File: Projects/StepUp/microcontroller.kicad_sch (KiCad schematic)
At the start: 1 part, among them U2 RP2040

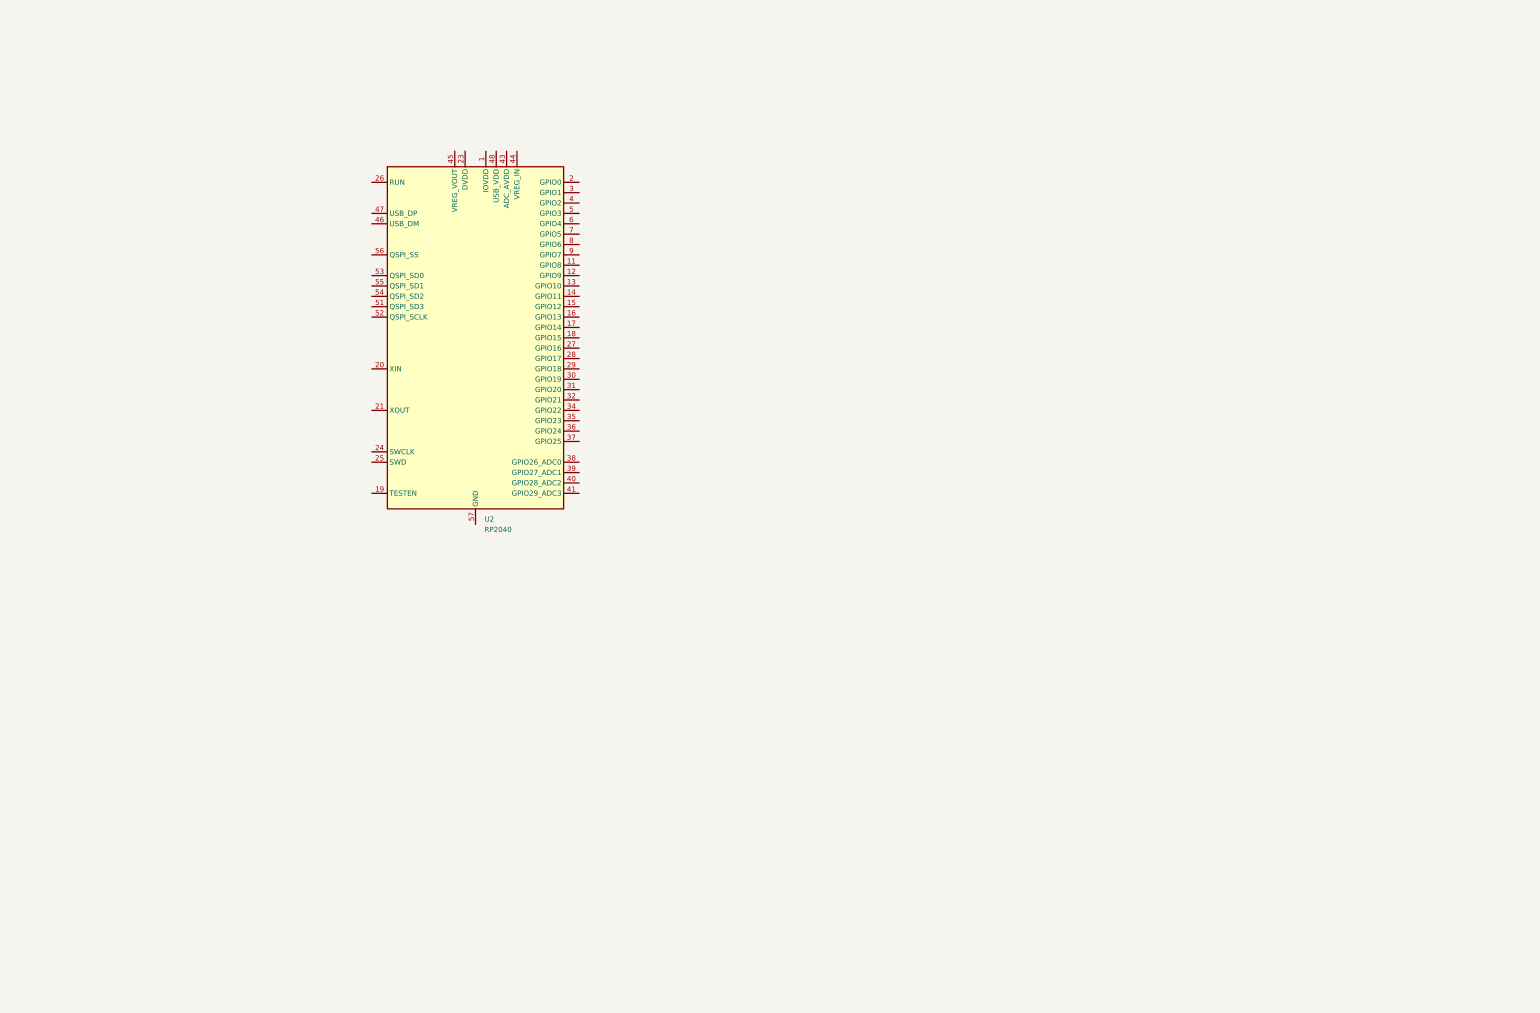
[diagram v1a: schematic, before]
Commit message: feat(rp2040): Layout begins, extra libraries
RPico minimal project downloaded + assets copied. Boost converter layout
in progress, 18650 battery holder added.
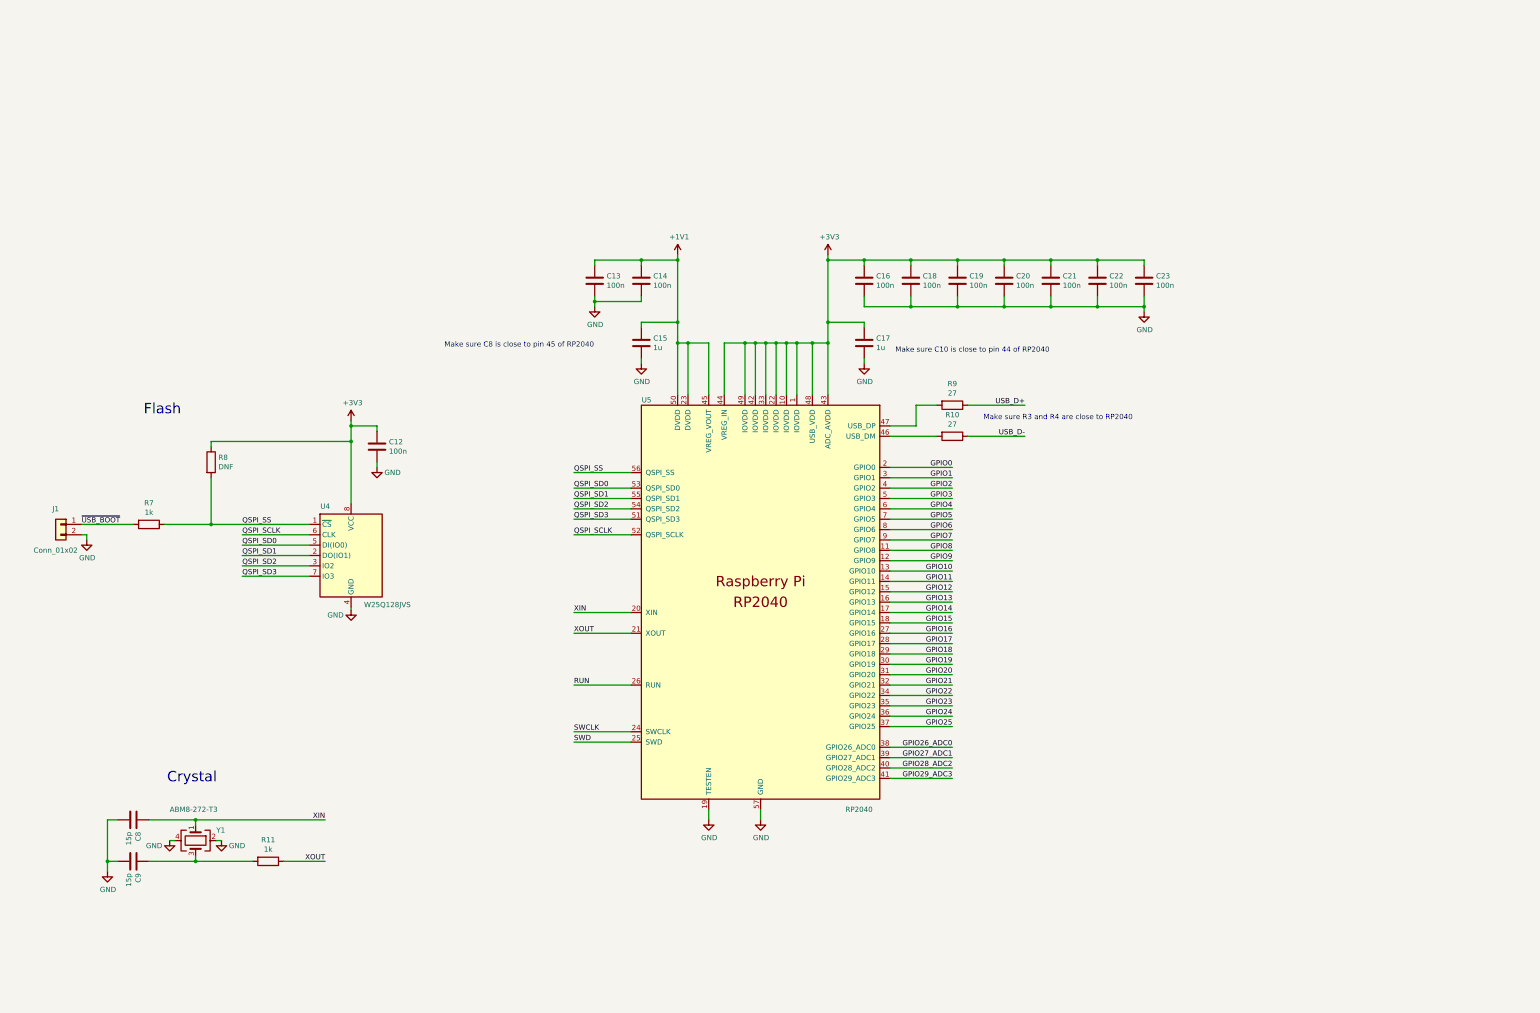
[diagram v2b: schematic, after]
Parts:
- removed U2: RP2040, Package_DFN_QFN:QFN-56-1EP_7x7mm_P0.4mm_EP3.2x3.2mm, symbol MCU_RaspberryPi:RP2040
- added C12, C13, C14, C16, C18, C19, C20, C21, C22, C23: 100n, Capacitor_SMD:C_0402_1005Metric, symbol Device:C
- added C15, C17: 1u, Capacitor_SMD:C_0402_1005Metric, symbol Device:C
- added C8, C9: 15p, Capacitor_SMD:C_0402_1005Metric, symbol Device:C
- added J1: Conn_01x02, Connector_PinHeader_2.54mm:PinHeader_1x02_P2.54mm_Vertical, symbol Connector_Generic:Conn_01x02
- added R10, R9: 27, Resistor_SMD:R_0402_1005Metric, symbol Device:R
- added R11, R7: 1k, Resistor_SMD:R_0402_1005Metric, symbol Device:R
- added R8: DNF, Resistor_SMD:R_0402_1005Metric, symbol Device:R
- added U4: W25Q128JVS, Package_SO:SOIC-8_5.23x5.23mm_P1.27mm, symbol Memory_Flash:W25Q128JVS
- added U5: RP2040, RP2040_minimal_r2:RP2040-QFN-56, symbol MCU_RaspberryPi_RP2040:RP2040
- added Y1: ABM8-272-T3, Crystal:Crystal_SMD_3225-4Pin_3.2x2.5mm, symbol Device:Crystal_GND24
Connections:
- new net: R10.2, U5.46 (USB_DM)
- new net: R9.2, U5.47 (USB_DP)
- new net: C9.1, R11.2, Y1.3
- new net +1V1: C13.1, C14.1, C15.1, U5.23 (DVDD), U5.45 (VREG_VOUT), U5.50 (DVDD)
- new net +3V3: C12.1, C16.1, C17.1, C18.1, C19.1, C20.1, C21.1, C22.1, C23.1, R8.1, U4.8 (VCC), U5.1 (IOVDD), U5.10 (IOVDD), U5.22 (IOVDD), U5.33 (IOVDD), U5.42 (IOVDD), U5.43 (ADC_AVDD), U5.44 (VREG_IN), U5.48 (USB_VDD), U5.49 (IOVDD)
- new net GND: C12.2, C13.2, C14.2, C15.2, C16.2, C17.2, C18.2, C19.2, C20.2, C21.2, C22.2, C23.2, C8.2, C9.2, J1.2 (Pin_2), U4.4 (GND), U5.19 (TESTEN), U5.57 (GND), Y1.2, Y1.4
- new net GPIO0: U5.2 (GPIO0)
- new net GPIO1: U5.3 (GPIO1)
- new net GPIO10: U5.13 (GPIO10)
- new net GPIO11: U5.14 (GPIO11)
- new net GPIO12: U5.15 (GPIO12)
- new net GPIO13: U5.16 (GPIO13)
- new net GPIO14: U5.17 (GPIO14)
- new net GPIO15: U5.18 (GPIO15)
- new net GPIO16: U5.27 (GPIO16)
- new net GPIO17: U5.28 (GPIO17)
- new net GPIO18: U5.29 (GPIO18)
- new net GPIO19: U5.30 (GPIO19)
- new net GPIO2: U5.4 (GPIO2)
- new net GPIO20: U5.31 (GPIO20)
- new net GPIO21: U5.32 (GPIO21)
- new net GPIO22: U5.34 (GPIO22)
- new net GPIO23: U5.35 (GPIO23)
- new net GPIO24: U5.36 (GPIO24)
- new net GPIO25: U5.37 (GPIO25)
- new net GPIO26_ADC0: U5.38 (GPIO26_ADC0)
- new net GPIO27_ADC1: U5.39 (GPIO27_ADC1)
- new net GPIO28_ADC2: U5.40 (GPIO28_ADC2)
- new net GPIO29_ADC3: U5.41 (GPIO29_ADC3)
- new net GPIO3: U5.5 (GPIO3)
- new net GPIO4: U5.6 (GPIO4)
- new net GPIO5: U5.7 (GPIO5)
- new net GPIO6: U5.8 (GPIO6)
- new net GPIO7: U5.9 (GPIO7)
- new net GPIO8: U5.11 (GPIO8)
- new net GPIO9: U5.12 (GPIO9)
- new net QSPI_SCLK: U4.6 (CLK), U5.52 (QSPI_SCLK)
- new net QSPI_SD0: U4.5 (DI(IO0)), U5.53 (QSPI_SD0)
- new net QSPI_SD1: U4.2 (DO(IO1)), U5.55 (QSPI_SD1)
- new net QSPI_SD2: U4.3 (IO2), U5.54 (QSPI_SD2)
- new net QSPI_SD3: U4.7 (IO3), U5.51 (QSPI_SD3)
- new net QSPI_SS: R7.1, R8.2, U4.1 (~{CS}), U5.56 (QSPI_SS)
- new net RUN: U5.26 (RUN)
- new net SWCLK: U5.24 (SWCLK)
- new net SWD: U5.25 (SWD)
- new net USB_D+: R9.1
- new net USB_D-: R10.1
- new net XIN: C8.1, U5.20 (XIN), Y1.1
- new net XOUT: R11.1, U5.21 (XOUT)
- new net ~{USB_BOOT}: J1.1 (Pin_1), R7.2
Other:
- note added: "Crystal"
- note added: "Flash"
- note added: "Make sure C10 is close to pin 44 of RP2040"
- note added: "Make sure C8 is close to pin 45 of RP2040"
- note added: "Make sure R3 and R4 are close to RP2040"

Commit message: feat(power): Input stage updates
USB vs Vbat source selection using PMOS gate logic.
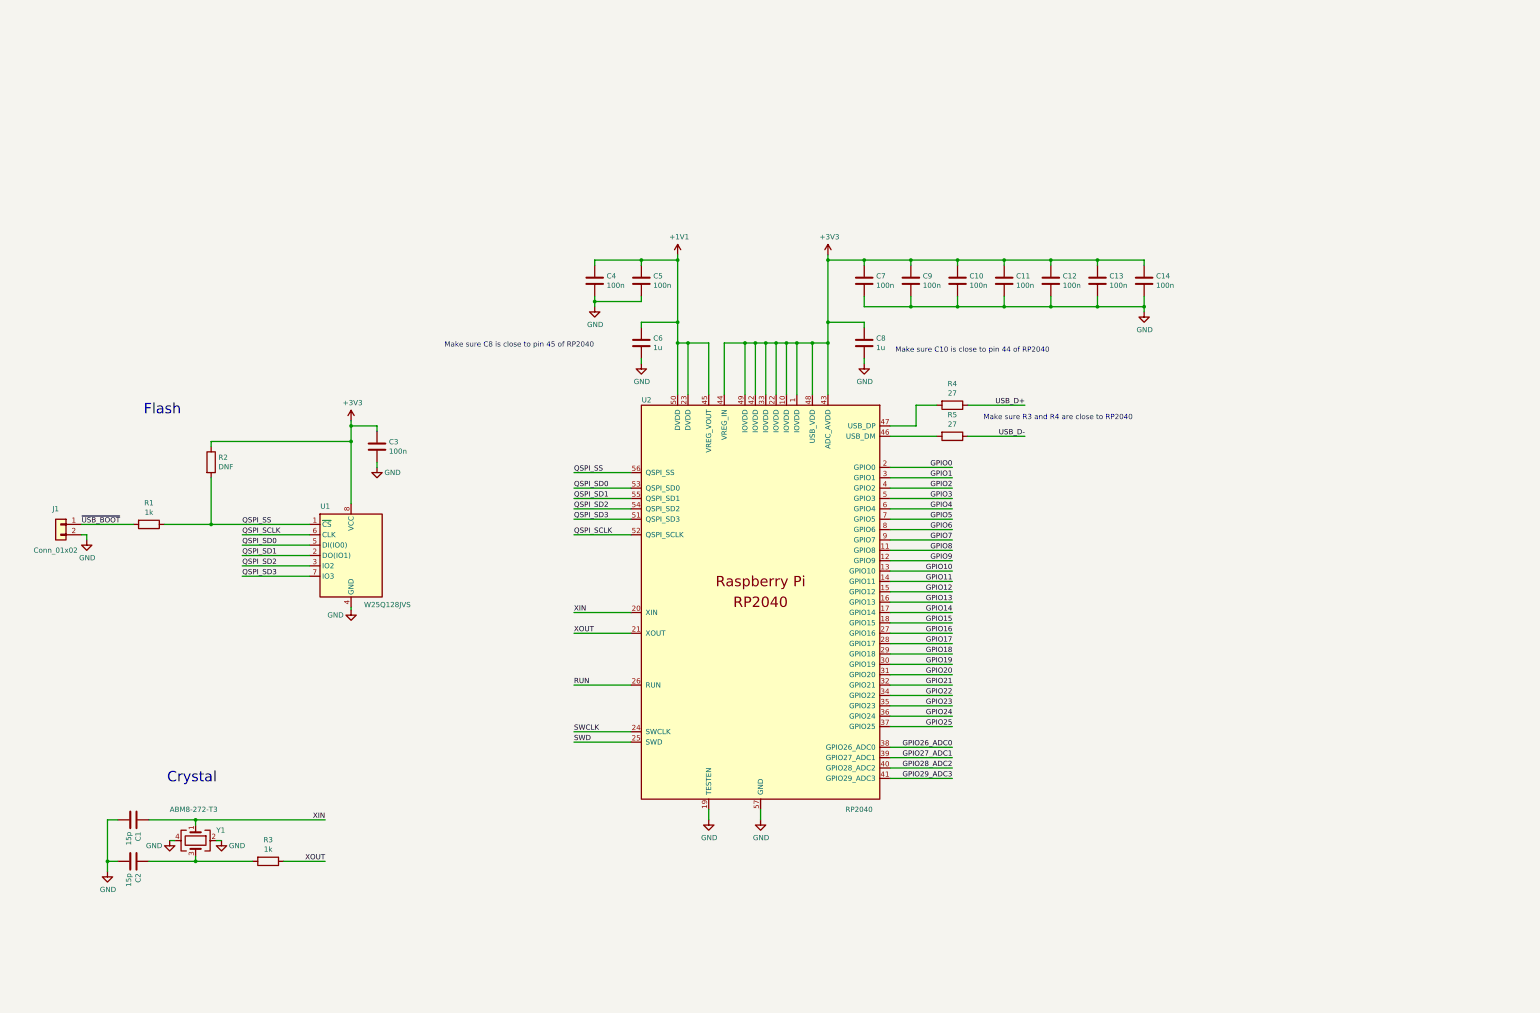
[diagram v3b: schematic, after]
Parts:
- renumbered C8 to C1, C19 to C10, C20 to C11, C21 to C12, C22 to C13, C23 to C14, C9 to C2, C12 to C3, C13 to C4, C14 to C5, C15 to C6, C16 to C7, C17 to C8, C18 to C9, R7 to R1, R8 to R2, R11 to R3, R9 to R4, R10 to R5, U4 to U1, U5 to U2

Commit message: feat(stepup): Many additions
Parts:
- removed J1: Conn_01x02, Connector_PinHeader_2.54mm:PinHeader_1x02_P2.54mm_Vertical, symbol Connector_Generic:Conn_01x02
- added D5: 1N4148W-TP, digikey-footprints:SOD-123, symbol dk_Diodes-Rectifiers-Single:1N4148W-TP
- added SW1, SW2: SW_Push, Button_Switch_SMD:SW_Push_1P1T_NO_Vertical_Wuerth_434133025816, symbol Switch:SW_Push
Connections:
- net GND: now also SW1.1, SW2.1
- net RUN: now also SW2.2
- net ~{USB_BOOT}: now also D5.A
- net GPIO22 renamed JOYSTSICK_BUTTON
- net GPIO25 renamed VUSB_monitor
- net GPIO26_ADC0 renamed JOYSTSICK_AXIS_V
- net GPIO27_ADC1 renamed JOYSTSICK_AXIS_H
- net GPIO28_ADC2 renamed Vbat_monitor
- new net: D5.K, SW1.2
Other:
- note added: "Flash memory"
- note added: "Make sure C6 is close to pin 45 of RP2040"
- note added: "Make sure these resistors are close to RP2040"
- note added: "Run - resets MCU USB_BOOT - hold this and toggle Run to enumerate as USB device for UF2 firmware upload"
- note removed: "Flash"
- note removed: "Make sure C8 is close to pin 45 of RP2040"
- note removed: "Make sure R3 and R4 are close to RP2040"
- moved on the sheet: C1, C2, C3, R1, R2, R3, U1, Y1

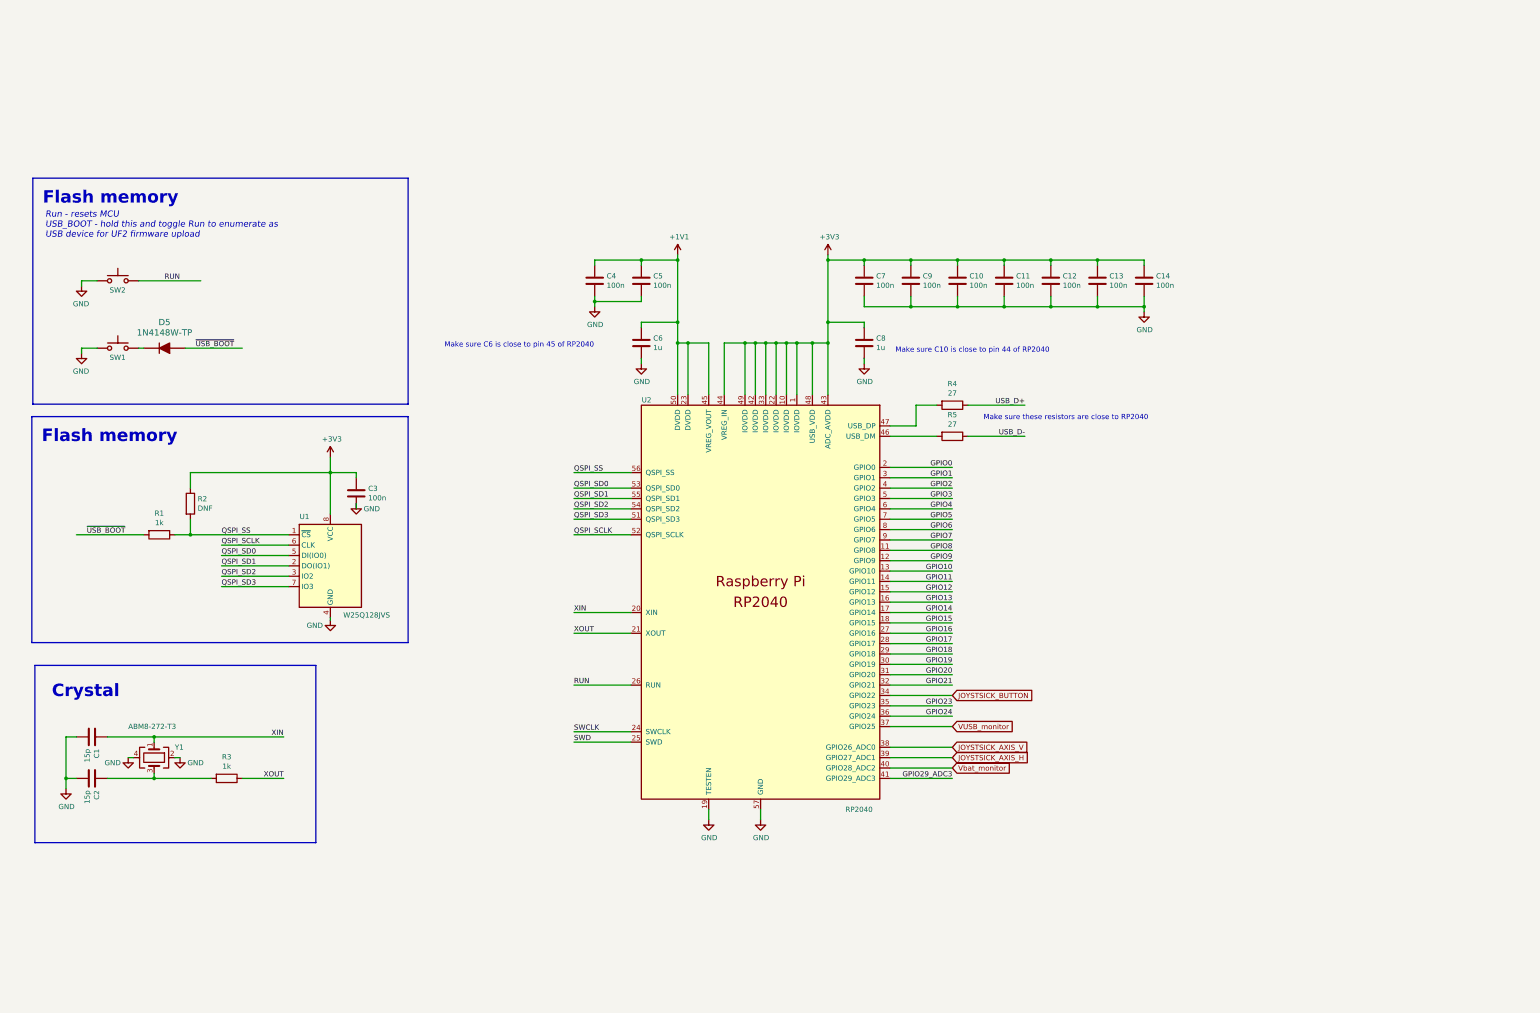
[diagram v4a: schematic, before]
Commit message: feat(stepup): Schematic + PCB updates
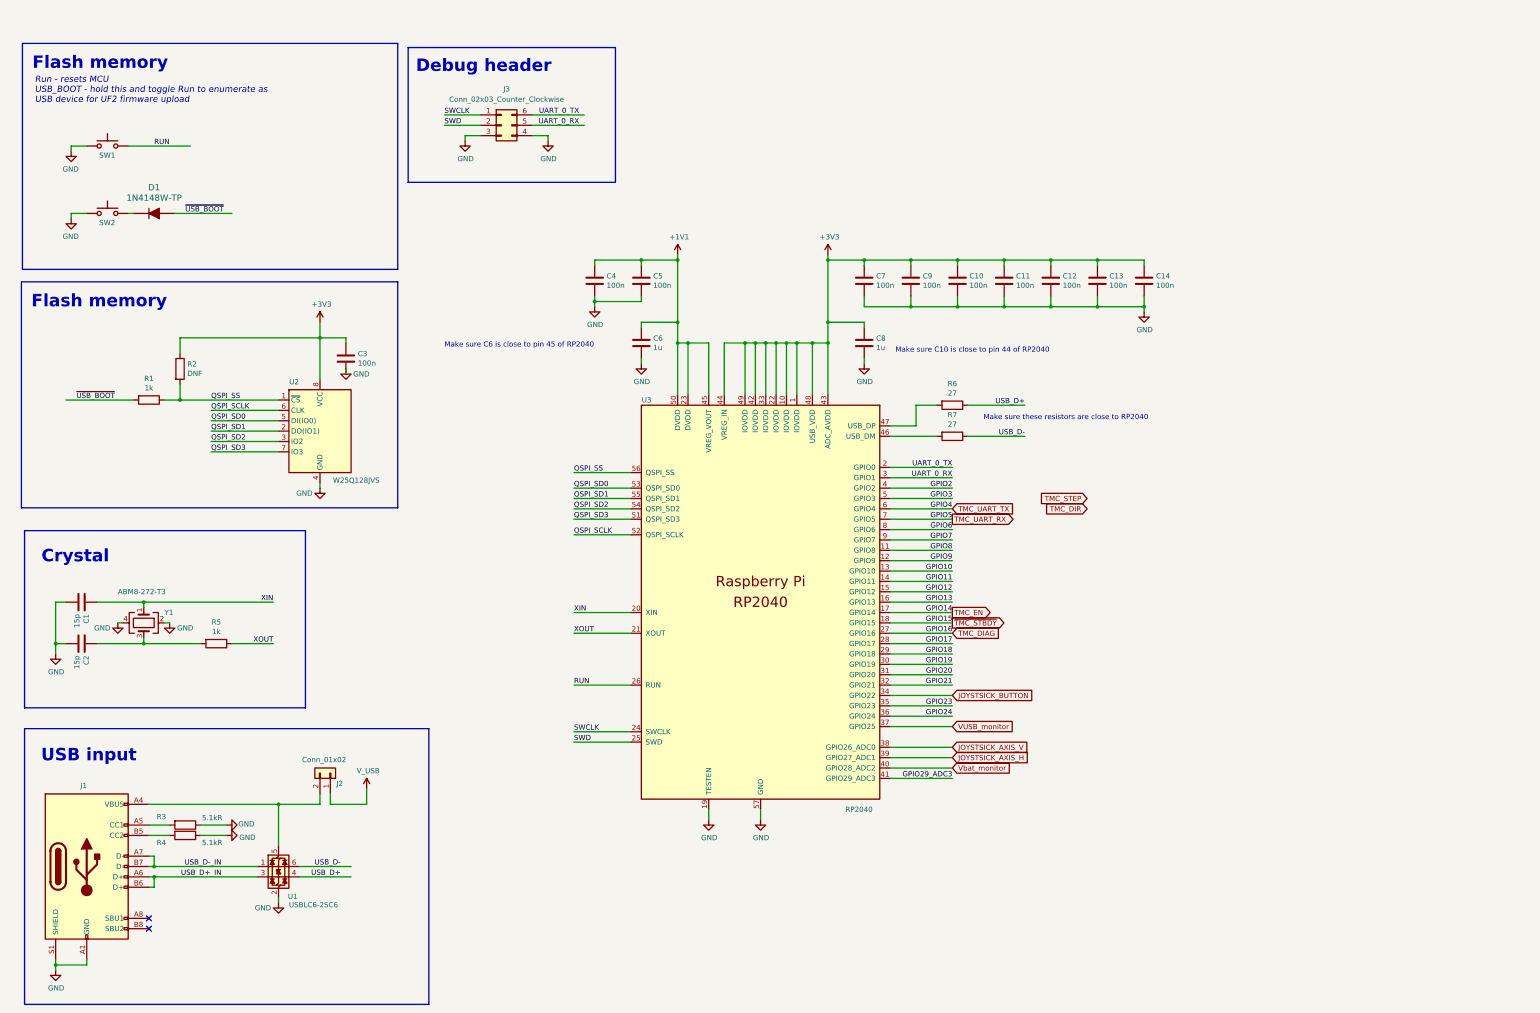
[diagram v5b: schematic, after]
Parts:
- added J1: USB_C_Receptacle_USB2.0_16P, Connector_USB:USB_C_Receptacle_GCT_USB4105-xx-A_16P_TopMnt_Horizontal, symbol Connector:USB_C_Receptacle_USB2.0_16P
- added J2: Conn_01x02, Connector_PinHeader_2.54mm:PinHeader_1x02_P2.54mm_Vertical, symbol Connector_Generic:Conn_01x02
- added J3: Conn_02x03_Counter_Clockwise, Connector_PinHeader_2.54mm:PinHeader_2x03_P2.54mm_Vertical, symbol Connector_Generic:Conn_02x03_Counter_Clockwise
- added R3, R4: 5.1kR, Resistor_SMD:R_0603_1608Metric, symbol Device:R
- added U1: USBLC6-2SC6, Package_TO_SOT_SMD:SOT-23-6, symbol Power_Protection:USBLC6-2SC6
- renumbered D5 to D1, R3 to R5, R4 to R6, R5 to R7, SW2 to SW1, SW1 to SW2, U1 to U2, U2 to U3
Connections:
- net GND: now also J1.A1 (GND), J1.A12 (GND), J1.B1 (GND), J1.B12 (GND), J1.S1 (SHIELD), J3.3 (Pin_3), J3.4 (Pin_4), R3.1, R4.1, U1.2 (GND)
- net SWCLK: now also J3.1 (Pin_1)
- net SWD: now also J3.2 (Pin_2)
- net USB_D+: now also U1.4 (I/O2)
- net USB_D-: now also U1.6 (I/O1)
- net GPIO0 renamed UART_0_TX
- net UART_0_TX: now also J3.6 (Pin_6)
- net GPIO1 renamed UART_0_RX
- net UART_0_RX: now also J3.5 (Pin_5)
- net GPIO14 renamed TMC_EN
- net GPIO15 renamed ~{TMC_STBDY}
- net GPIO16 renamed TMC_DIAG
- net GPIO4 renamed TMC_UART_TX
- net GPIO5 renamed TMC_UART_RX
- new net: J1.B5 (CC2), R4.2
- new net: J1.A4 (VBUS), J1.A9 (VBUS), J1.B4 (VBUS), J1.B9 (VBUS), J2.2 (Pin_2), U1.5 (VBUS)
- new net: J1.A5 (CC1), R3.2
- new net USB_D+_IN: J1.A6 (D+), J1.B6 (D+), U1.3 (I/O2)
- new net USB_D-_IN: J1.A7 (D-), J1.B7 (D-), U1.1 (I/O1)
- new net V_USB: J2.1 (Pin_1)
- no-connect marks 0 -> 2
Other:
- note added: "Debug header"
- note added: "USB input"
- moved on the sheet: C1, C2, C3, D1, R1, R2, R5, SW1, SW2, U2, Y1
